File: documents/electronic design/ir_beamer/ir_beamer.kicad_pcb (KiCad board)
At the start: 2 copper layers, 23 parts, among them U11 74HC595D, U11 SE8R01_module, U11 STM32F103HEADER

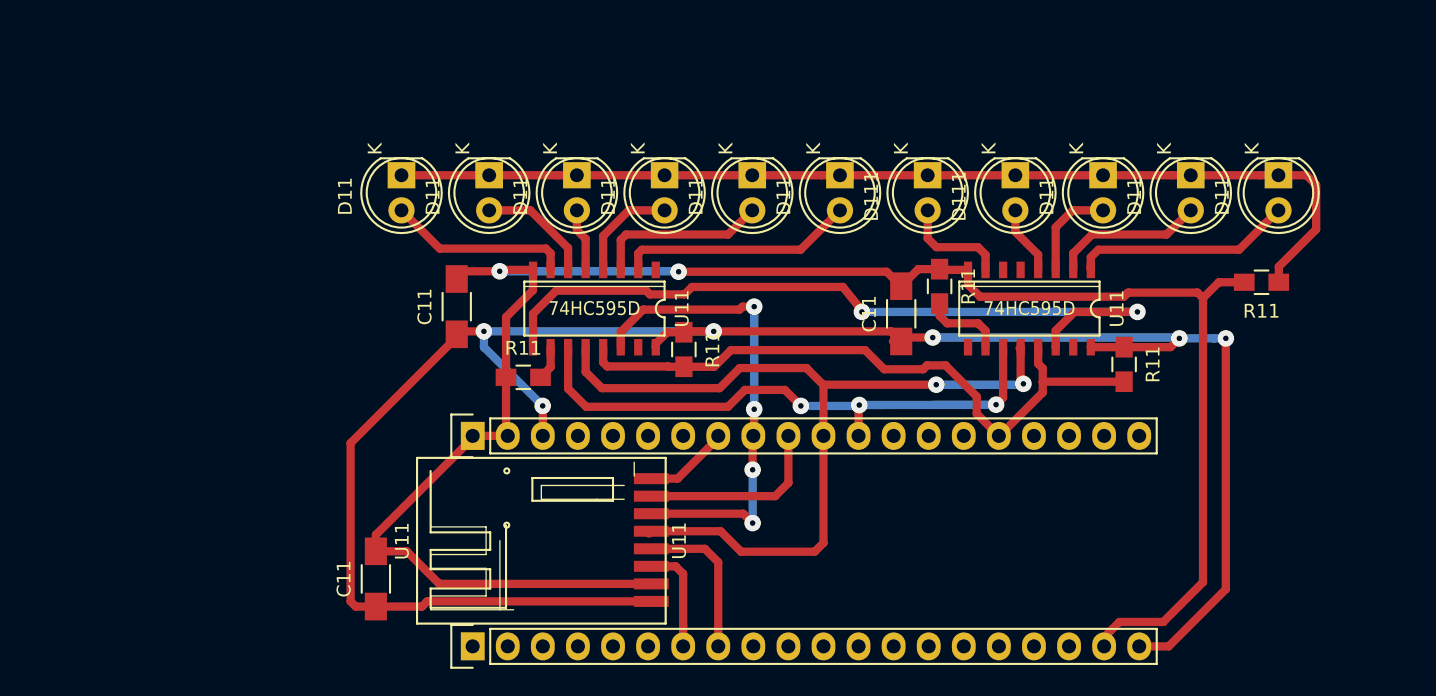
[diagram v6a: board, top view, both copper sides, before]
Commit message: make pcb for 11 leds
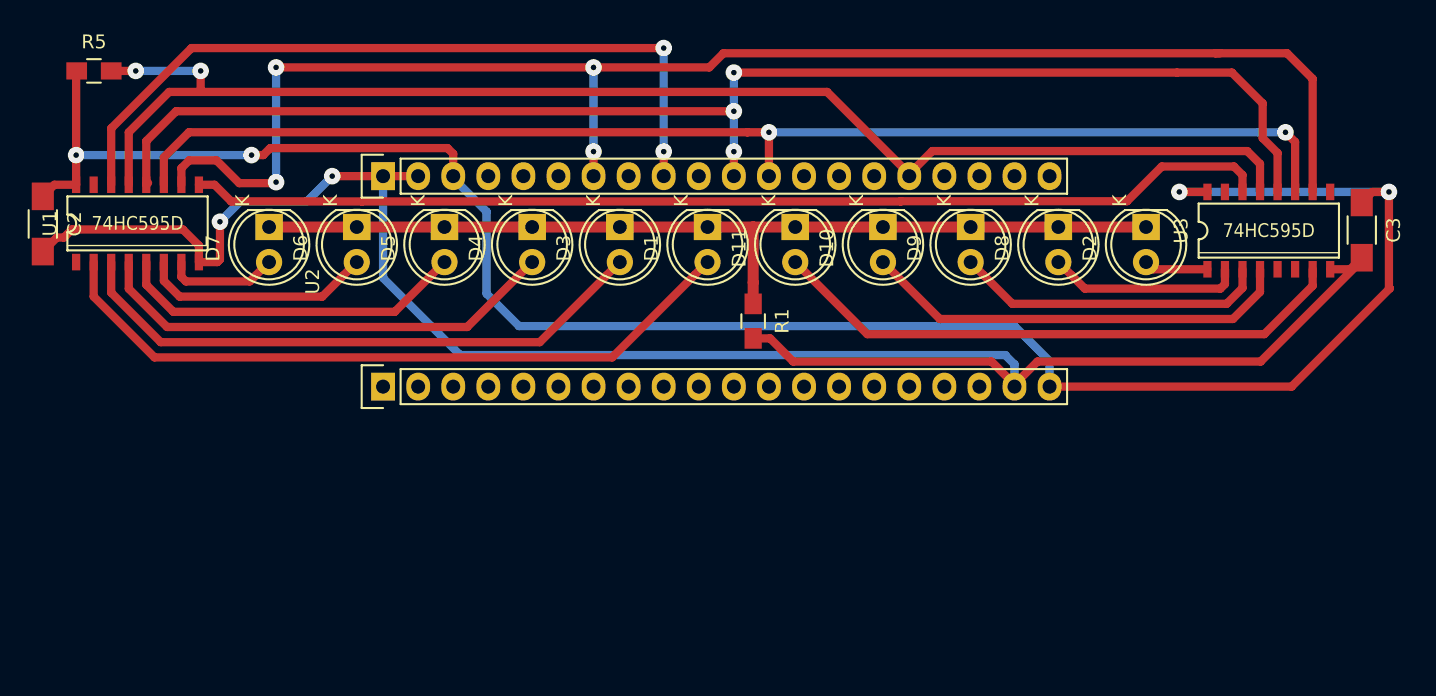
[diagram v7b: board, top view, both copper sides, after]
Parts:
- removed C11 (x3): 100uf, Capacitors_SMD:C_1206_HandSoldering
- removed the D11 at (80.6, 28.6)
- removed the D11 at (112.4, 28.6)
- removed the D11 at (74.3, 28.6)
- removed the D11 at (67.9, 28.6)
- removed the D11 at (61.6, 28.6)
- removed the D11 at (55.2, 28.6)
- removed the D11 at (48.9, 28.6)
- removed the D11 at (106.0, 28.6)
- removed the D11 at (99.7, 28.6)
- removed D111 (x2): LED, LEDs:LED-5MM
- removed R11 (x4): 10K, Capacitors_SMD:C_0805_HandSoldering
- removed R11: 22, Capacitors_SMD:C_0805_HandSoldering
- removed U11 (x2): 74HC595D, footprints:74HC595D_SO16
- removed U11: STM32F103HEADER, footprints:STM32F103_header_footprint
- removed U11: SE8R01_module, footprints:SE8R01_SMD
- added C2: 100uf, Capacitors_SMD:C_1206_HandSoldering, F.Cu at (22.9, 32.1)
- added C3: 100uf, Capacitors_SMD:C_1206_HandSoldering, F.Cu at (118.4, 32.5)
- added D1: LED, LEDs:LED-5MM, F.Cu at (71.1, 32.3)
- added D10: LED, LEDs:LED-5MM, F.Cu at (83.8, 32.3)
- added D11: LED, LEDs:LED-5MM, F.Cu at (77.4, 32.3)
- added D2: LED, LEDs:LED-5MM, F.Cu at (102.8, 32.3)
- added D3: LED, LEDs:LED-5MM, F.Cu at (64.7, 32.3)
- added D4: LED, LEDs:LED-5MM, F.Cu at (58.4, 32.3)
- added D5: LED, LEDs:LED-5MM, F.Cu at (52.0, 32.3)
- added D6: LED, LEDs:LED-5MM, F.Cu at (45.7, 32.3)
- added D7: LED, LEDs:LED-5MM, F.Cu at (39.3, 32.3)
- added D8: LED, LEDs:LED-5MM, F.Cu at (96.5, 32.3)
- added D9: LED, LEDs:LED-5MM, F.Cu at (90.1, 32.3)
- added R1: 22, Capacitors_SMD:C_0805_HandSoldering, F.Cu at (74.4, 39.1)
- added R5: 10K, Capacitors_SMD:C_0805_HandSoldering, F.Cu at (26.6, 21.0)
- added U1: 74HC595D, footprints:74HC595D_SO16, F.Cu at (29.8, 32.1)
- added U2: STM32F103HEADER, footprints:STM32F103_header_footprint, F.Cu at (47.6, 43.9)
- added U3: 74HC595D, footprints:74HC595D_SO16, F.Cu at (111.7, 32.6)
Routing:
- net MR_NOT: track 0.00 -> 110.1 mm, vias 0 -> 4
- net IR_PWM: track 48.7 -> 100.6 mm, vias 0 -> 2
- net Latch: track 42.2 -> 91.7 mm, vias 3 -> 2
- net SPI_SCK: track 63.9 -> 100.4 mm, vias 2 -> 3
- net IR_LED_2: track 17.1 -> 51.6 mm
- net IR_LED_DATA: track 7.81 -> 42.3 mm
- net IR_LED_3: track 12.6 -> 42.9 mm
- net IR_LED_4: track 7.67 -> 34.2 mm
- net IR_LED_10: track 5.05 -> 31.5 mm
- net Cascade: track 55.8 -> 78.6 mm, vias 2 -> 0
- net IR_LED_5: track 4.58 -> 25.5 mm
- net SPI_MOSI: track 35.1 -> 55.8 mm, vias 4 -> 2
- net IR_LED_9: track 7.29 -> 22.8 mm
- net SPI_MISO: track 13.7 -> 0.00 mm
- net IR_LED_1: track 16.2 -> 4.66 mm
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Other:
- net class Default: clearance 0.4 -> 0.5
- rule trace_clearance: 0.4 -> 0.5

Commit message: update pcb for beamer
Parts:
- removed the C2 at (22.9, 32.1)
- removed the C3 at (118.4, 32.5)
- removed the D1 at (71.1, 32.3)
- removed the D10 at (83.8, 32.3)
- removed the D11 at (77.4, 32.3)
- removed the D2 at (102.8, 32.3)
- removed the D3 at (64.7, 32.3)
- removed the D4 at (58.4, 32.3)
- removed the D5 at (52.0, 32.3)
- removed the D6 at (45.7, 32.3)
- removed the D7 at (39.3, 32.3)
- removed the D8 at (96.5, 32.3)
- removed the D9 at (90.1, 32.3)
- removed the R1 at (74.4, 39.1)
- removed the R5 at (26.6, 21.0)
- removed the U1 at (29.8, 32.1)
- removed the U2 at (47.6, 43.9)
- removed the U3 at (111.7, 32.6)
- added C1: 100uf, Capacitors_SMD:C_1206_HandSoldering, F.Cu at (258.0, 110.3)
- added C1: 100uf, Capacitors_SMD:C_1206_HandSoldering, B.Cu at (233.8, 110.4)
- added C1: 100uf, Capacitors_SMD:C_1206_HandSoldering, B.Cu at (153.8, 110.4)
- added C1: 100uf, Capacitors_SMD:C_1206_HandSoldering, F.Cu at (179.3, 110.3)
- added C1: 100uf, Capacitors_SMD:C_1206_HandSoldering, F.Cu at (99.3, 110.3)
- added C1: 100uf, Capacitors_SMD:C_1206_HandSoldering, B.Cu at (73.8, 110.4)
- added C1: 100uf, Capacitors_SMD:C_1206_HandSoldering, F.Cu at (19.3, 110.3)
- added C2: 100uf, Capacitors_SMD:C_1206_HandSoldering, F.Cu at (256.5, 25.0)
- added C2: 100uf, Capacitors_SMD:C_1206_HandSoldering, B.Cu at (235.4, 25.0)
- added C2: 100uf, Capacitors_SMD:C_1206_HandSoldering, B.Cu at (155.4, 25.0)
- added C2: 100uf, Capacitors_SMD:C_1206_HandSoldering, F.Cu at (177.7, 25.0)
- added C2: 100uf, Capacitors_SMD:C_1206_HandSoldering, F.Cu at (97.7, 25.0)
- added C2: 100uf, Capacitors_SMD:C_1206_HandSoldering, B.Cu at (75.4, 25.0)
- added C2: 100uf, Capacitors_SMD:C_1206_HandSoldering, F.Cu at (17.7, 25.0)
- added C3: 100uf, Capacitors_SMD:C_1206_HandSoldering, F.Cu at (273.0, 38.2)
- added C3: 100uf, Capacitors_SMD:C_1206_HandSoldering, B.Cu at (218.8, 38.3)
- added C3: 100uf, Capacitors_SMD:C_1206_HandSoldering, B.Cu at (138.8, 38.3)
- added C3: 100uf, Capacitors_SMD:C_1206_HandSoldering, F.Cu at (194.3, 38.2)
- added C3: 100uf, Capacitors_SMD:C_1206_HandSoldering, F.Cu at (114.3, 38.2)
- added C3: 100uf, Capacitors_SMD:C_1206_HandSoldering, B.Cu at (58.8, 38.3)
- added C3: 100uf, Capacitors_SMD:C_1206_HandSoldering, F.Cu at (34.3, 38.2)
- added D1: LED, LEDs:LED-5MM, F.Cu at (254.1, 74.0)
- added D1: LED, LEDs:LED-5MM, B.Cu at (237.7, 74.1)
- added D1: LED, LEDs:LED-5MM, B.Cu at (157.7, 74.1)
- added D1: LED, LEDs:LED-5MM, F.Cu at (175.4, 74.0)
- added D1: LED, LEDs:LED-5MM, F.Cu at (95.4, 74.0)
- added D1: LED, LEDs:LED-5MM, B.Cu at (77.7, 74.1)
- added D1: LED, LEDs:LED-5MM, F.Cu at (15.4, 74.0)
- added D10: LED, LEDs:LED-5MM, F.Cu at (254.1, 61.3)
- added D10: LED, LEDs:LED-5MM, B.Cu at (237.7, 61.4)
- added D10: LED, LEDs:LED-5MM, B.Cu at (157.7, 61.4)
- added D10: LED, LEDs:LED-5MM, F.Cu at (175.4, 61.3)
- added D10: LED, LEDs:LED-5MM, F.Cu at (95.4, 61.3)
- added D10: LED, LEDs:LED-5MM, B.Cu at (77.7, 61.4)
- added D10: LED, LEDs:LED-5MM, F.Cu at (15.4, 61.3)
- added D11: LED, LEDs:LED-5MM, F.Cu at (254.1, 67.6)
- added D11: LED, LEDs:LED-5MM, B.Cu at (237.7, 67.7)
- added D11: LED, LEDs:LED-5MM, B.Cu at (157.7, 67.7)
- added D11: LED, LEDs:LED-5MM, F.Cu at (175.4, 67.6)
- added D11: LED, LEDs:LED-5MM, F.Cu at (95.4, 67.6)
- added D11: LED, LEDs:LED-5MM, B.Cu at (77.7, 67.7)
- added D11: LED, LEDs:LED-5MM, F.Cu at (15.4, 67.6)
- added D2: LED, LEDs:LED-5MM, F.Cu at (254.1, 42.2)
- added D2: LED, LEDs:LED-5MM, B.Cu at (237.7, 42.3)
- added D2: LED, LEDs:LED-5MM, B.Cu at (157.7, 42.3)
- added D2: LED, LEDs:LED-5MM, F.Cu at (175.4, 42.2)
- added D2: LED, LEDs:LED-5MM, F.Cu at (95.4, 42.2)
- added D2: LED, LEDs:LED-5MM, B.Cu at (77.7, 42.3)
- added D2: LED, LEDs:LED-5MM, F.Cu at (15.4, 42.2)
- added D3: LED, LEDs:LED-5MM, F.Cu at (254.1, 80.3)
- added D3: LED, LEDs:LED-5MM, B.Cu at (237.7, 80.4)
- added D3: LED, LEDs:LED-5MM, B.Cu at (157.7, 80.4)
- added D3: LED, LEDs:LED-5MM, F.Cu at (175.4, 80.3)
- added D3: LED, LEDs:LED-5MM, F.Cu at (95.4, 80.3)
- added D3: LED, LEDs:LED-5MM, B.Cu at (77.7, 80.4)
- added D3: LED, LEDs:LED-5MM, F.Cu at (15.4, 80.3)
- added D4: LED, LEDs:LED-5MM, F.Cu at (254.1, 86.7)
- added D4: LED, LEDs:LED-5MM, B.Cu at (237.7, 86.8)
- added D4: LED, LEDs:LED-5MM, B.Cu at (157.7, 86.8)
- added D4: LED, LEDs:LED-5MM, F.Cu at (175.4, 86.7)
- added D4: LED, LEDs:LED-5MM, F.Cu at (95.4, 86.7)
- added D4: LED, LEDs:LED-5MM, B.Cu at (77.7, 86.8)
- added D4: LED, LEDs:LED-5MM, F.Cu at (15.4, 86.7)
- added D5: LED, LEDs:LED-5MM, F.Cu at (254.1, 93.0)
- added D5: LED, LEDs:LED-5MM, B.Cu at (237.7, 93.1)
- added D5: LED, LEDs:LED-5MM, B.Cu at (157.7, 93.1)
- added D5: LED, LEDs:LED-5MM, F.Cu at (175.4, 93.0)
- added D5: LED, LEDs:LED-5MM, F.Cu at (95.4, 93.0)
- added D5: LED, LEDs:LED-5MM, B.Cu at (77.7, 93.1)
- added D5: LED, LEDs:LED-5MM, F.Cu at (15.4, 93.0)
- added D6: LED, LEDs:LED-5MM, F.Cu at (254.1, 99.4)
- added D6: LED, LEDs:LED-5MM, B.Cu at (237.7, 99.5)
- added D6: LED, LEDs:LED-5MM, B.Cu at (157.7, 99.5)
- added D6: LED, LEDs:LED-5MM, F.Cu at (175.4, 99.4)
- added D6: LED, LEDs:LED-5MM, F.Cu at (95.4, 99.4)
- added D6: LED, LEDs:LED-5MM, B.Cu at (77.7, 99.5)
- added D6: LED, LEDs:LED-5MM, F.Cu at (15.4, 99.4)
- added D7: LED, LEDs:LED-5MM, F.Cu at (254.1, 105.7)
- added D7: LED, LEDs:LED-5MM, B.Cu at (237.7, 105.8)
- added D7: LED, LEDs:LED-5MM, B.Cu at (157.7, 105.8)
- added D7: LED, LEDs:LED-5MM, F.Cu at (175.4, 105.7)
- added D7: LED, LEDs:LED-5MM, F.Cu at (95.4, 105.7)
- added D7: LED, LEDs:LED-5MM, B.Cu at (77.7, 105.8)
- added D7: LED, LEDs:LED-5MM, F.Cu at (15.4, 105.7)
- added D8: LED, LEDs:LED-5MM, F.Cu at (254.1, 48.6)
- added D8: LED, LEDs:LED-5MM, B.Cu at (237.7, 48.7)
- added D8: LED, LEDs:LED-5MM, B.Cu at (157.7, 48.7)
- added D8: LED, LEDs:LED-5MM, F.Cu at (175.4, 48.6)
- added D8: LED, LEDs:LED-5MM, F.Cu at (95.4, 48.6)
- added D8: LED, LEDs:LED-5MM, B.Cu at (77.7, 48.7)
- added D8: LED, LEDs:LED-5MM, F.Cu at (15.4, 48.6)
- added D9: LED, LEDs:LED-5MM, F.Cu at (254.1, 54.9)
- added D9: LED, LEDs:LED-5MM, B.Cu at (237.7, 55.0)
- added D9: LED, LEDs:LED-5MM, B.Cu at (157.7, 55.0)
- added D9: LED, LEDs:LED-5MM, F.Cu at (175.4, 54.9)
- added D9: LED, LEDs:LED-5MM, F.Cu at (95.4, 54.9)
- added D9: LED, LEDs:LED-5MM, B.Cu at (77.7, 55.0)
- added D9: LED, LEDs:LED-5MM, F.Cu at (15.4, 54.9)
- added R1: 22, Capacitors_SMD:C_0805_HandSoldering, F.Cu at (253.3, 111.1)
- added R1: 22, Capacitors_SMD:C_0805_HandSoldering, B.Cu at (238.6, 111.2)
- added R1: 22, Capacitors_SMD:C_0805_HandSoldering, B.Cu at (158.6, 111.2)
- added R1: 22, Capacitors_SMD:C_0805_HandSoldering, F.Cu at (174.5, 111.1)
- added R1: 22, Capacitors_SMD:C_0805_HandSoldering, F.Cu at (94.5, 111.1)
- added R1: 22, Capacitors_SMD:C_0805_HandSoldering, B.Cu at (78.6, 111.2)
- added R1: 22, Capacitors_SMD:C_0805_HandSoldering, F.Cu at (14.5, 111.1)
- added R5: 10K, Capacitors_SMD:C_0805_HandSoldering, F.Cu at (268.2, 86.4)
- added R5: 10K, Capacitors_SMD:C_0805_HandSoldering, B.Cu at (223.7, 86.5)
- added R5: 10K, Capacitors_SMD:C_0805_HandSoldering, B.Cu at (143.7, 86.5)
- added R5: 10K, Capacitors_SMD:C_0805_HandSoldering, F.Cu at (189.4, 86.4)
- added R5: 10K, Capacitors_SMD:C_0805_HandSoldering, F.Cu at (109.4, 86.4)
- added R5: 10K, Capacitors_SMD:C_0805_HandSoldering, B.Cu at (63.7, 86.5)
- added R5: 10K, Capacitors_SMD:C_0805_HandSoldering, F.Cu at (29.4, 86.4)
- added U1: 74HC595D, footprints:74HC595D_SO16, F.Cu at (265.2, 105.0)
- added U1: 74HC595D, footprints:74HC595D_SO16, B.Cu at (226.6, 105.1)
- added U1: 74HC595D, footprints:74HC595D_SO16, B.Cu at (146.6, 105.1)
- added U1: 74HC595D, footprints:74HC595D_SO16, F.Cu at (186.4, 105.0)
- added U1: 74HC595D, footprints:74HC595D_SO16, F.Cu at (106.4, 105.0)
- added U1: 74HC595D, footprints:74HC595D_SO16, B.Cu at (66.6, 105.1)
- added U1: 74HC595D, footprints:74HC595D_SO16, F.Cu at (26.4, 105.0)
- added U2: STM32F103HEADER, footprints:STM32F103_header_footprint, F.Cu at (278.1, 96.7)
- added U2: STM32F103HEADER, footprints:STM32F103_header_footprint, B.Cu at (213.7, 96.8)
- added U2: STM32F103HEADER, footprints:STM32F103_header_footprint, B.Cu at (133.7, 96.8)
- added U2: STM32F103HEADER, footprints:STM32F103_header_footprint, F.Cu at (199.4, 96.7)
- added U2: STM32F103HEADER, footprints:STM32F103_header_footprint, F.Cu at (119.4, 96.7)
- added U2: STM32F103HEADER, footprints:STM32F103_header_footprint, B.Cu at (53.7, 96.8)
- added U2: STM32F103HEADER, footprints:STM32F103_header_footprint, F.Cu at (39.4, 96.7)
- added U3: 74HC595D, footprints:74HC595D_SO16, F.Cu at (265.2, 40.2)
- added U3: 74HC595D, footprints:74HC595D_SO16, B.Cu at (226.6, 40.3)
- added U3: 74HC595D, footprints:74HC595D_SO16, B.Cu at (146.6, 40.3)
- added U3: 74HC595D, footprints:74HC595D_SO16, F.Cu at (186.4, 40.2)
- added U3: 74HC595D, footprints:74HC595D_SO16, F.Cu at (106.4, 40.2)
- added U3: 74HC595D, footprints:74HC595D_SO16, B.Cu at (66.6, 40.3)
- added U3: 74HC595D, footprints:74HC595D_SO16, F.Cu at (26.4, 40.2)
- added U4: SE8R01_module, SE8R01, F.Cu at (260.3, 22.4)
- added U4: SE8R01_module, SE8R01, B.Cu at (231.5, 22.5)
- added U4: SE8R01_module, SE8R01, B.Cu at (151.5, 22.5)
- added U4: SE8R01_module, SE8R01, F.Cu at (181.6, 22.4)
- added U4: SE8R01_module, SE8R01, F.Cu at (101.6, 22.4)
- added U4: SE8R01_module, SE8R01, B.Cu at (71.5, 22.5)
- added U4: SE8R01_module, SE8R01, F.Cu at (21.6, 22.4)
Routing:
- net GND: track 143.2 -> 1226.9 mm, vias 2 -> 42
- net +3V3: track 148.6 -> 1215.1 mm, vias 4 -> 35
- net SPI_SCK: track 100.4 -> 793.6 mm, vias 3 -> 42
- net SPI_MOSI: track 55.8 -> 642.8 mm, vias 2 -> 28
- net IR_PWM: track 100.6 -> 588.1 mm, vias 2 -> 21
- net RADIO_CE: track 0.00 -> 470.4 mm
- net Cascade: track 78.6 -> 542.1 mm
- net Latch: track 91.7 -> 537.0 mm, vias 2 -> 14
- net RADIO_CSN: track 0.00 -> 437.7 mm
- net RADIO_IRQ: track 0.00 -> 435.4 mm, vias 0 -> 14
- net MR_NOT: track 110.1 -> 543.1 mm, vias 4 -> 14
- net IR_GND: track 69.1 -> 476.0 mm
- net SPI_MISO: track 0.00 -> 355.2 mm, vias 0 -> 14
- net IR_LED_2: track 51.6 -> 216.1 mm
- net IR_LED_DATA: track 42.3 -> 190.4 mm
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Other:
- net class Default: via_drill 0.4 -> 0.5
- net class IR_GND: via_drill 0.4 -> 0.5
- net class IR_SIGNAL added: clearance 0.5, trace_width 0.4, via_dia 1.2, via_drill 0.5
- net class RADIO added: clearance 0.5, trace_width 0.5, via_dia 1.2, via_drill 0.5
